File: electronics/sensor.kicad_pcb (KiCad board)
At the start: 2 copper layers, 96 x 48 mm, 37 parts, among them CON1 MOTOR_PWR, J1 EXP. IN, J2 EXP. OUT, P1 CONN_01X05, P10 CONN_01X04, P2 CONN_01X05, P3 CONN_01X05, P4 CONN_01X05, P5 SENSOR, P6 CONN_01X04, P7 CONN_01X04, P8 CONN_01X04, P9 SENSOR, U1 arduino_uno_shield, U10 GP2S60, U2 MIC5842, U3 74HC165, U4 MIC5842, U5 WS2812B, U6 WS2812B, U7 WS2812B, U8 WS2812B, U9 GP2S60

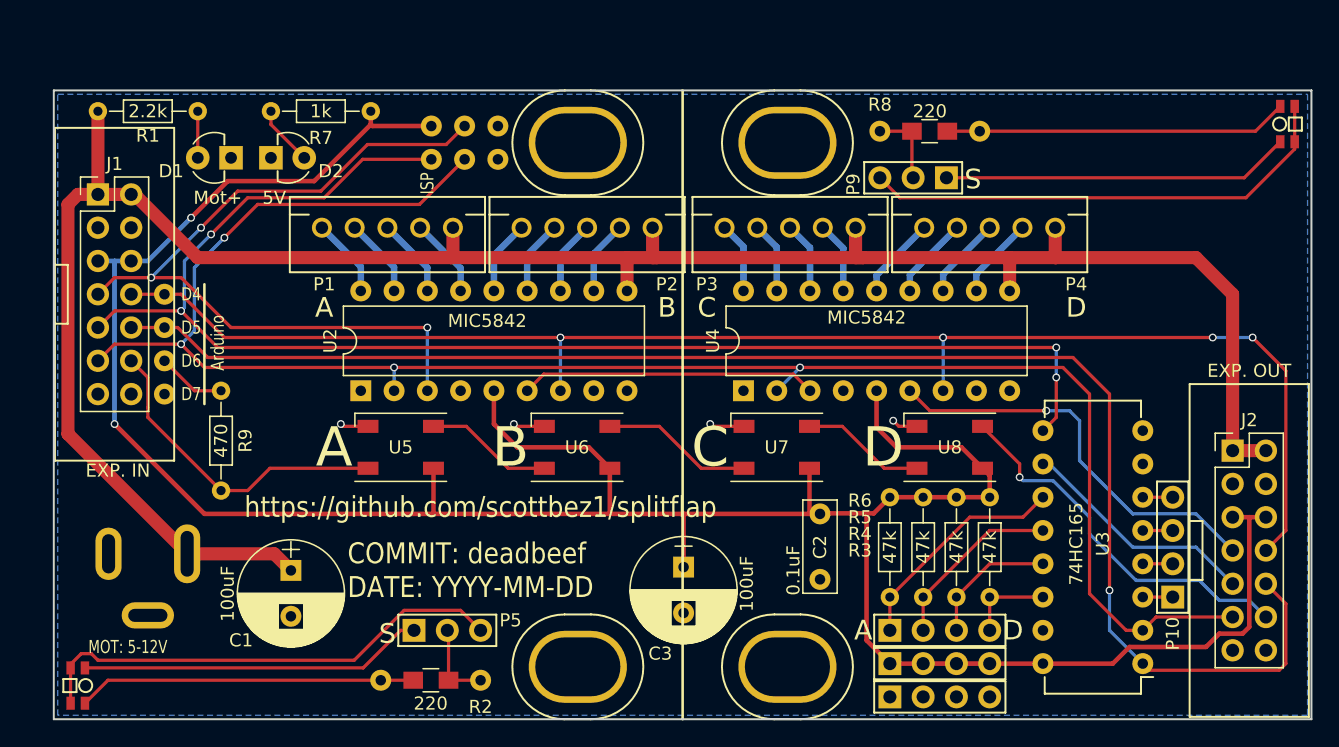
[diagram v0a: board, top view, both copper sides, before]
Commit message: Sensor schematic, starting pcb
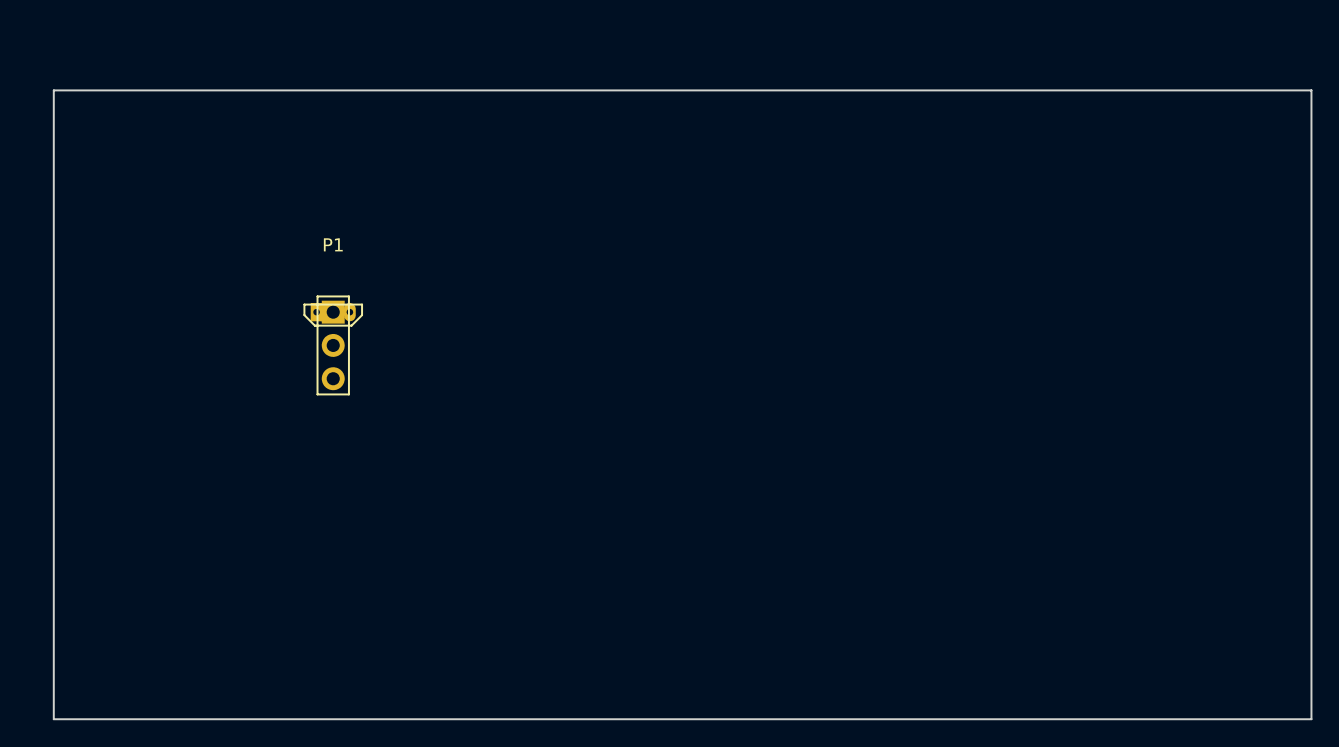
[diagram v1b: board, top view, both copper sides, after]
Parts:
- removed C1, C3: 100uF, Capacitors_ThroughHole:CP_Radial_D8.0mm_P3.50mm
- removed C2: 0.1uF, Capacitors_ThroughHole:C_Rect_L7.0mm_W2.5mm_P5.00mm
- removed CON1: MOTOR_PWR, PJ-202A:PJ-202A
- removed D1: Mot+, LED3mmBetterSilkScreen:LED_D3.0mm
- removed D2: 5V, LED3mmBetterSilkScreen:LED_D3.0mm
- removed J1: EXP. IN, PinHeaders:Pin_Header_Straight_2x07_Pitch2.54mm_IDC_Shrouded
- removed J2: EXP. OUT, PinHeaders:Pin_Header_Straight_2x07_Pitch2.54mm_IDC_Shrouded
- removed P10, P6, P7, P8: CONN_01X04, PinHeaders:Pin_Header_Straight_1x04
- removed P2, P3, P4: CONN_01X05, JST_XH_Connectors:JST_XH_2-5mm_5pin
- removed P5, P9: SENSOR, PinHeaders:Pin_Header_Straight_1x03
- removed R1: 2.2k, Resistors_ThroughHole:R_Axial_DIN0204_L3.6mm_D1.6mm_P7.62mm_Horizontal
- removed R2, R8: 220, Resistor0805ThroughHole:R_0805_ThroughHole
- removed R3, R4, R5, R6: 47k, Resistors_ThroughHole:R_Axial_DIN0204_L3.6mm_D1.6mm_P7.62mm_Horizontal
- removed R7: 1k, Resistors_ThroughHole:R_Axial_DIN0204_L3.6mm_D1.6mm_P7.62mm_Horizontal
- removed R9: 470, Resistors_ThroughHole:R_Axial_DIN0204_L3.6mm_D1.6mm_P7.62mm_Horizontal
- removed U10, U9: GP2S60, GP2S60:GP2S60_WITH_MOUNT
- removed U2, U4: MIC5842, Housings_DIP:DIP-18_W7.62mm
- removed U3: 74HC165, Housings_DIP:DIP-16_W7.62mm
- removed U5, U6, U7, U8: WS2812B, LEDs:LED_WS2812B-PLCC4
- P1: value CONN_01X05 -> SENSOR; footprint JST_XH_Connectors:JST_XH_2-5mm_5pin -> PinHeaders:Pin_Header_Straight_1x03
- U1: value arduino_uno_shield -> AH1815; footprint ArduinoUnoShield:arduino_uno_shield -> ah1815:AH1815
- moved U1 64.3 mm to (41.3, 36.9), turned to 0 degrees
- moved P1 7.66 mm to (41.3, 36.9)
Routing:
- net +5V: track 212.8 -> 0.00 mm, vias 2 -> 0
- net VCC: track 167.5 -> 0.00 mm
- net /SPI_CLOCK: track 140.1 -> 0.00 mm, vias 4 -> 0
- net /SENSOR_LATCH: track 116.5 -> 0.00 mm, vias 1 -> 0
- net /MOTOR_LATCH: track 113.0 -> 0.00 mm, vias 4 -> 0
- net /SENSOR_DATA_OUT: track 107.6 -> 0.00 mm, vias 4 -> 0
- net /MOTOR_DATA_IN: track 60.8 -> 0.00 mm, vias 3 -> 0
- net Net-(P9-Pad3): track 37.1 -> 0.00 mm
- net Net-(P5-Pad3): track 37.0 -> 0.00 mm
- net /MOTOR_DATA_OUT: track 31.5 -> 0.00 mm, vias 1 -> 0
- net /DBGLED_OUT: track 29.0 -> 0.00 mm, vias 1 -> 0
- net Net-(P9-Pad1): track 26.6 -> 0.00 mm
- net Net-(P5-Pad1): track 26.3 -> 0.00 mm
- net Net-(R8-Pad2): track 26.2 -> 0.00 mm
- net Net-(R2-Pad2): track 25.8 -> 0.00 mm
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- removed copper zone on B.Cu, net GND
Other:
- board text removed: "A"
- board text removed: "Arduino"
- board text removed: "B"
- board text removed: "C"
- board text removed: "COMMIT: deadbeef DATE: YYYY-MM-DD"
- board text removed: "D"
- board text removed: "D4"
- board text removed: "D5"
- board text removed: "D6"
- board text removed: "D7"
- board text removed: "ISP"
- board text removed: "MOT: 5-12V"
- board text removed: "S"
- board text removed: "https://github.com/scottbez1/splitflap"

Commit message: Initial reasonable sensor breakout
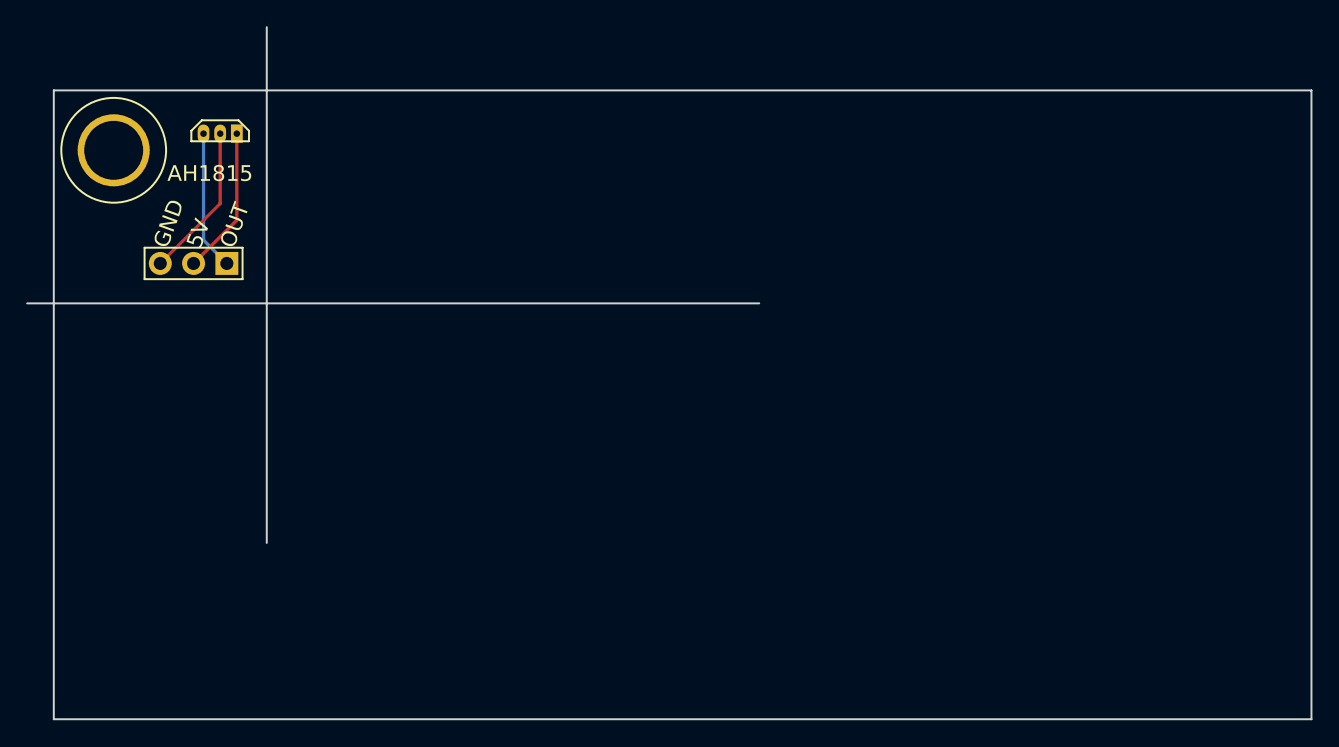
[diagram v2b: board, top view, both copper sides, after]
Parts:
- added Z1: MOUNT, MountingHoles:M4_mount, F.Cu at (24.6, 24.6)
- U1: moved to B.Cu
- moved U1 16.1 mm to (32.7, 23.3), turned to 180 degrees
- moved P1 8.93 mm to (33.2, 33.2), turned to 270 degrees
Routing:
- net Net-(P1-Pad3): track 0.00 -> 11.8 mm
- net Net-(P1-Pad2): track 0.00 -> 11.3 mm
- net Net-(P1-Pad1): track 0.00 -> 10.6 mm
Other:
- board size 96 x 48 mm -> 98 x 52.8 mm
- board text added: "5V"
- board text added: "AH1815"
- board text added: "GND"
- board text added: "OUT"
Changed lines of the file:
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@@
   (general
     (links 3)
-    (no_connects 3)
+    (no_connects 0)
     (area 19.924999 19.924999 116.075001 68.075001)
     (thickness 1.6)
-    (drawings 4)
-    (tracks 0)
+    (drawings 10)
+    (tracks 6)
     (zones 0)
-    (modules 2)
+    (modules 3)
     (nets 4)
   )
@@
     (pad_to_mask_clearance 0.2)
     (aux_axis_origin 0 0)
+    (grid_origin 20 20)
     (visible_elements FFFFFF7F)
     (pcbplotparams
@@
   )
   (module PinHeaders:Pin_Header_Straight_1x03 (layer F.Cu)
-    (at 41.33 36.927001)
+    (at 33.208 33.208 270)
     (descr "Through hole pin header")
     (tags "pin header")
-    (fp_text reference P1 (at 0 -5.1) (layer F.SilkS)
-      (effects (font (size 1 1) (thickness 0.15)))
-    )
-    (fp_text value SENSOR (at 0 -3.1) (layer F.Fab)
+    (fp_text reference P1 (at -2.032 0 360) (layer F.SilkS) hide
+      (effects (font (size 1 1) (thickness 0.15)))
+    )
+    (fp_text value SENSOR (at -2.032 4.318 360) (layer F.Fab) hide
       (effects (font (size 1 1) (thickness 0.15)))
     )
@@
     (fp_line (start 1.2 -1.2) (end 1.2 6.28) (layer F.SilkS) (width 0.15))
     (fp_line (start -1.2 -1.2) (end 1.2 -1.2) (layer F.SilkS) (width 0.15))
-    (pad 1 thru_hole rect (at 0 0) (size 1.75 1.75) (drill 1) (layers *.Cu *.Mask F.SilkS)
+    (pad 1 thru_hole rect (at 0 0 270) (size 1.75 1.75) (drill 1) (layers *.Cu *.Mask F.SilkS)
       (net 3 "Net-(P1-Pad1)"))
-    (pad 2 thru_hole circle (at 0 2.54) (size 1.75 1.75) (drill 1) (layers *.Cu *.Mask F.SilkS)
+    (pad 2 thru_hole circle (at 0 2.54 270) (size 1.75 1.75) (drill 1) (layers *.Cu *.Mask F.SilkS)
       (net 2 "Net-(P1-Pad2)"))
-    (pad 3 thru_hole circle (at 0 5.08) (size 1.75 1.75) (drill 1) (layers *.Cu *.Mask F.SilkS)
+    (pad 3 thru_hole circle (at 0 5.08 270) (size 1.75 1.75) (drill 1) (layers *.Cu *.Mask F.SilkS)
       (net 1 "Net-(P1-Pad3)"))
     (model Pin_Headers.3dshapes/Pin_Header_Straight_1x03.wrl
@@
     )
   )
-  (module ah1815:AH1815 (layer F.Cu)
-    (at 41.33 36.927001)
-    (fp_text reference U1 (at 5.08 -1.27) (layer F.SilkS) hide
-      (effects (font (size 1 1) (thickness 0.15)))
-    )
-    (fp_text value AH1815 (at 0 -2.54) (layer F.Fab)
-      (effects (font (size 1 1) (thickness 0.15)))
-    )
-    (fp_line (start -1.4 1.03) (end 1.4 1.03) (layer F.SilkS) (width 0.15))
-    (fp_line (start 2.2 0.23) (end 1.4 1.03) (layer F.SilkS) (width 0.15))
-    (fp_line (start -2.2 0.23) (end -1.4 1.03) (layer F.SilkS) (width 0.15))
+  (module MountingHoles:M4_mount (layer F.Cu)
+    (at 24.572 24.572)
+    (fp_text reference Z1 (at 0 1.7) (layer F.SilkS) hide
+      (effects (font (size 1 1) (thickness 0.15)))
+    )
+    (fp_text value MOUNT (at 0 -1.5) (layer F.Fab) hide
+      (effects (font (size 1 1) (thickness 0.15)))
+    )
+    (fp_circle (center 0 0) (end 4 0) (layer F.SilkS) (width 0.15))
+    (pad 1 thru_hole circle (at 0 0) (size 5.5 5.5) (drill 4.5) (layers *.Cu *.Mask F.SilkS)
+      (clearance 1.5))
+  )
+  (module ah1815:AH1815 (layer B.Cu)
+    (at 32.7 23.302 180)
+    (fp_text reference U1 (at 5.08 1.27 180) (layer B.SilkS) hide
+      (effects (font (size 1 1) (thickness 0.15)) (justify mirror))
+    )
+    (fp_text value AH1815 (at 0 2.54 180) (layer B.Fab) hide
+      (effects (font (size 1 1) (thickness 0.15)) (justify mirror))
+    )
+    (fp_line (start 2.2 -0.58) (end -2.2 -0.58) (layer F.SilkS) (width 0.15))
     (fp_line (start 2.2 0.22) (end 2.2 -0.58) (layer F.SilkS) (width 0.15))
     (fp_line (start -2.2 0.22) (end -2.2 -0.58) (layer F.SilkS) (width 0.15))
-    (fp_line (start -2.2 -0.58) (end 2.2 -0.58) (layer F.SilkS) (width 0.15))
-    (pad 1 thru_hole rect (at -1.27 0) (size 0.9 1.4) (drill 0.5) (layers *.Cu *.Mask)
+    (fp_line (start 2.2 0.22) (end 1.4 1.02) (layer F.SilkS) (width 0.15))
+    (fp_line (start -2.2 0.22) (end -1.4 1.02) (layer F.SilkS) (width 0.15))
+    (fp_line (start 1.4 1.02) (end -1.4 1.02) (layer F.SilkS) (width 0.15))
+    (fp_line (start -1.4 -1.02) (end 1.4 -1.03) (layer B.SilkS) (width 0.15))
+    (fp_line (start 2.2 -0.22) (end 1.4 -1.02) (layer B.SilkS) (width 0.15))
+    (fp_line (start -2.2 -0.22) (end -1.4 -1.02) (layer B.SilkS) (width 0.15))
+    (fp_line (start 2.2 -0.22) (end 2.2 0.58) (layer B.SilkS) (width 0.15))
+    (fp_line (start -2.2 -0.22) (end -2.2 0.58) (layer B.SilkS) (width 0.15))
+    (fp_line (start -2.2 0.58) (end 2.2 0.58) (layer B.SilkS) (width 0.15))
+    (pad 1 thru_hole rect (at -1.27 0 180) (size 0.9 1.4) (drill 0.5) (layers *.Cu *.Mask)
       (net 2 "Net-(P1-Pad2)"))
-    (pad 2 thru_hole oval (at 0 0) (size 0.9 1.4) (drill 0.5) (layers *.Cu *.Mask)
+    (pad 2 thru_hole oval (at 0 0 180) (size 0.9 1.4) (drill 0.5) (layers *.Cu *.Mask)
       (net 1 "Net-(P1-Pad3)"))
-    (pad 3 thru_hole oval (at 1.27 0) (size 0.9 1.4) (drill 0.5) (layers *.Cu *.Mask)
+    (pad 3 thru_hole oval (at 1.27 0 180) (size 0.9 1.4) (drill 0.5) (layers *.Cu *.Mask)
       (net 3 "Net-(P1-Pad1)"))
   )
+  (gr_text AH1815 (at 31.938 26.35) (layer F.SilkS)
+    (effects (font (size 1.2 1.2) (thickness 0.24)))
+  )
+  (gr_text OUT (at 33.208 31.938 70) (layer F.SilkS)
+    (effects (font (size 1.2 1.2) (thickness 0.25)) (justify left))
+  )
+  (gr_text 5V (at 30.668 31.938 70) (layer F.SilkS)
+    (effects (font (size 1.2 1.2) (thickness 0.25)) (justify left))
+  )
+  (gr_text GND (at 28.128 31.938 70) (layer F.SilkS)
+    (effects (font (size 1.2 1.2) (thickness 0.25)) (justify left))
+  )
+  (gr_line (start 36.256 15.174) (end 36.256 54.544) (angle 90) (layer Edge.Cuts) (width 0.15))
+  (gr_line (start 17.968 36.256) (end 73.848 36.256) (angle 90) (layer Edge.Cuts) (width 0.15))
   (gr_line (start 116 20) (end 116 68) (angle 90) (layer Edge.Cuts) (width 0.15))
   (gr_line (start 20 68) (end 20 20) (angle 90) (layer Edge.Cuts) (width 0.15))
   (gr_line (start 116 68) (end 20 68) (angle 90) (layer Edge.Cuts) (width 0.15))
   (gr_line (start 20 20) (end 116 20) (angle 90) (layer Edge.Cuts) (width 0.15))
+  (segment (start 32.7 23.302) (end 32.7 28.636) (width 0.25) (layer F.Cu) (net 1))
+  (segment (start 32.7 28.636) (end 28.128 33.208) (width 0.25) (layer F.Cu) (net 1))
+  (segment (start 33.97 23.302) (end 33.97 29.906) (width 0.25) (layer F.Cu) (net 2))
+  (segment (start 33.97 29.906) (end 30.668 33.208) (width 0.25) (layer F.Cu) (net 2))
+  (segment (start 31.43 23.302) (end 31.43 31.43) (width 0.25) (layer B.Cu) (net 3))
+  (segment (start 31.43 31.43) (end 33.208 33.208) (width 0.25) (layer B.Cu) (net 3))
 )
